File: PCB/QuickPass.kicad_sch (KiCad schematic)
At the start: 8 parts, among them J1 USB_A, J2 Conn_01x04_Female, SW1 SW_MEC_5E, SW2 SW_Push, SW3 SW_Push, SW4 RotaryEncoder_Switch, SW5 SW_MEC_5E, U1 KB2040

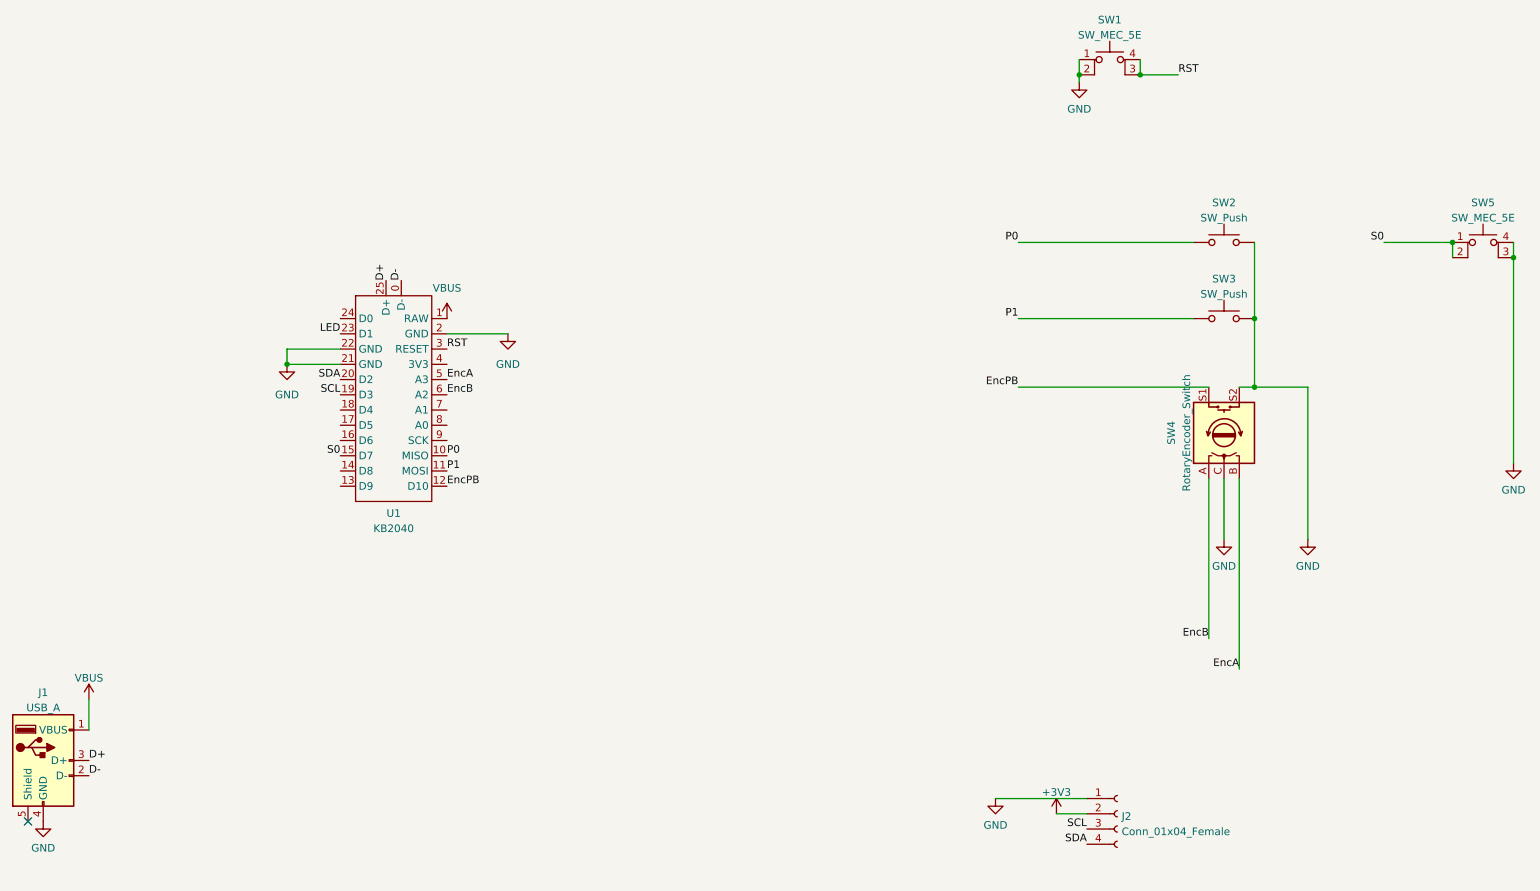
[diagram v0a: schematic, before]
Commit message: separate PCB switch and MCU
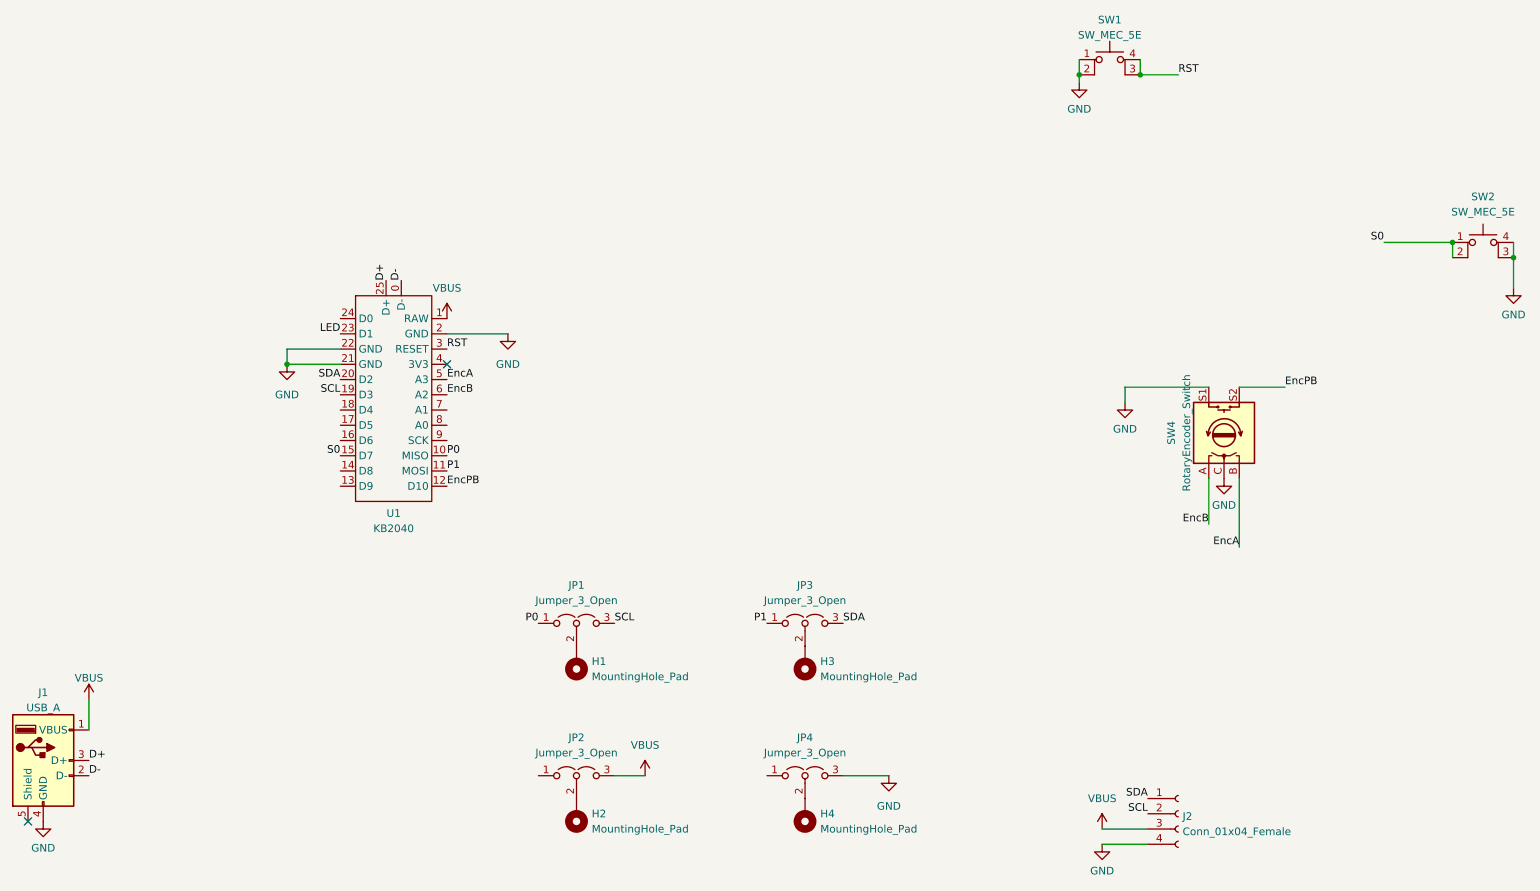
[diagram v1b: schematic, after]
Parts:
- removed SW2, SW3: SW_Push, Button_Switch_Keyboard:SW_Cherry_MX_1.00u_PCB, symbol Switch:SW_Push
- added H1, H2, H3, H4: MountingHole_Pad, MountingHole:MountingHole_2.2mm_M2_DIN965_Pad, symbol Mechanical:MountingHole_Pad
- added JP1, JP2, JP3, JP4: Jumper_3_Open, Jumper:SolderJumper-3_P2.0mm_Open_TrianglePad1.0x1.5mm, symbol Jumper:Jumper_3_Open
- renumbered SW5 to SW2
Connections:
- net +3V3 is gone; now on net SCL: J2.2 (Pin_2)
- net EncPB: now also SW4.S2; no longer SW4.S1
- net GND: now also J2.4 (Pin_4), SW4.S1, JP4.3 (B); no longer J2.1 (Pin_1), SW4.S2
- net P0: now also JP1.1 (A)
- net P1: now also JP3.1 (A)
- net SCL: now also JP1.3 (B); no longer J2.3 (Pin_3)
- net SDA: now also J2.1 (Pin_1), JP3.3 (B); no longer J2.4 (Pin_4)
- net VBUS: now also J2.3 (Pin_3), JP2.3 (B)
- new net: H2.1, JP2.2 (C)
- new net: H4.1, JP4.2 (C)
- new net: H3.1, JP3.2 (C)
- new net: H1.1, JP1.2 (C)
- no-connect marks 1 -> 2
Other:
- moved on the sheet: J2

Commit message: add lower plate
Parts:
- removed JP1, JP2, JP3, JP4: Jumper_3_Open, Jumper:SolderJumper-3_P2.0mm_Open_TrianglePad1.0x1.5mm, symbol Jumper:Jumper_3_Open
- added R1, R2: 10k, Resistor_SMD:R_0603_1608Metric, symbol Device:R
- SW1, SW2: footprint QMK:THAU13-AB-R -> Akizuki:THAU13-AB-R
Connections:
- net EncPB: now also U1.9 (SCK); no longer U1.12 (D10)
- net GND: now also H2.1, H4.1
- net P0: now also H1.1, U1.7 (A1); no longer U1.10 (MISO)
- net P1: now also H3.1, U1.8 (A0); no longer U1.11 (MOSI)
- net SCL: now also U1.17 (D5), R2.2; no longer U1.19 (D3)
- net SDA: now also U1.18 (D4), R1.2; no longer U1.20 (D2)
- net VBUS: now also R1.1, R2.1
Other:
- moved on the sheet: H1, H2, H3, H4
